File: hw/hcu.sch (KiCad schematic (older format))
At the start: 2 parts, among them J101 AMPSEAL_23_POS_VERT_BLACK_SEA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, J102 AMPSEAL_8_POS_VERT_BLACK_SEAL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

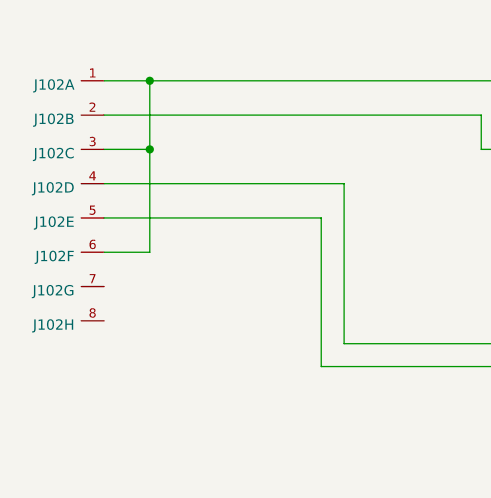
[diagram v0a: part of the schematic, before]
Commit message: ampseal 8 pin changed to white one
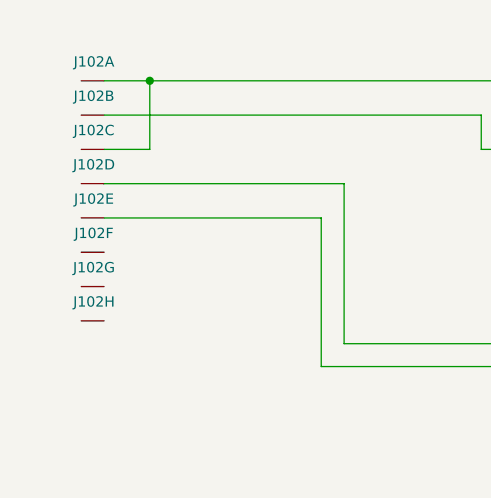
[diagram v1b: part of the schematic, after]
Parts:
- removed J102: AMPSEAL_8_POS_VERT_BLACK_SEALED_1-776276-1, usevolt:AMPSEAL_8_POS_776275-1, symbol usevolt:AMPSEAL_8_POS_VERT_BLACK_SEALED_1-776276-1
- added J102: AMPSEAL_8_POS_VERT_WHITE_SEALED_1-776276-2, usevolt:AMPSEAL_8_POS_776275-1, symbol usevolt:AMPSEAL_8_POS_VERT_WHITE_SEALED_1-776276-2
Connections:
- net Power supply/GND: now also J102.2 (S)
- net Power supply/VIN: now also J102.1 (S), J102.3 (S)
- net lpc1549/CANH: now also J102.4 (S)
- net lpc1549/CANL: now also J102.5 (S)

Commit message: pcb 1.3.0 created
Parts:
- added R1: 120, yageo:0603, symbol yageo:120
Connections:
- net lpc1549/CANH: now also R1.1 (R1)
- net lpc1549/CANL: now also R1.2 (R2)
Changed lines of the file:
@@
 	5150 3900 5150 3250
 Wire Wire Line
-	5150 3250 2500 3250
+	5150 3250 4350 3250
 Wire Wire Line
 	2500 3250 2500 2550
@@
 	2400 2700 2400 3350
 Wire Wire Line
-	2400 3350 5050 3350
+	2400 3350 4050 3350
 Wire Wire Line
 	5050 3350 5050 4000
@@
 	-1   0    0    1
 $EndComp
+$Comp
+L yageo:120 R1
+U 1 1 5C4A75DD
+P 4150 3600
+F 0 "R1" H 4200 3784 45  0000 C CNN
+F 1 "120" H 4200 3700 45  0000 C CNN
+F 2 "yageo:0603" H 4180 3750 20  0001 C CNN
+F 3 "" H 4119 3639 60  0001 C CNN
+F 4 "" H 4519 4039 60  0001 C CNN "1st Source Part Number"
+F 5 "Digikey" H 4419 3939 60  0001 C CNN "1st Source"
+F 6 "RC0603FR-07120RL" H 4319 3839 60  0001 C CNN "Manufacturer Part Number"
+F 7 "YAGEO" H 4219 3739 60  0001 C CNN "Manufacturer"
+	1    4150 3600
+	1    0    0    -1
+$EndComp
+Wire Wire Line
+	4050 3600 4050 3350
+Connection ~ 4050 3350
+Wire Wire Line
+	4050 3350 5050 3350
+Wire Wire Line
+	4350 3600 4350 3250
+Connection ~ 4350 3250
+Wire Wire Line
+	4350 3250 2500 3250
 $EndSCHEMATC
